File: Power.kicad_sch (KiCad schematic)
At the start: 30 parts, among them J201 Screw_Terminal_01x02_P5mm, J202 USB-C_304A-ACP16X, U201 TPS5430DDA, U202 NUCLEO64-H503RB

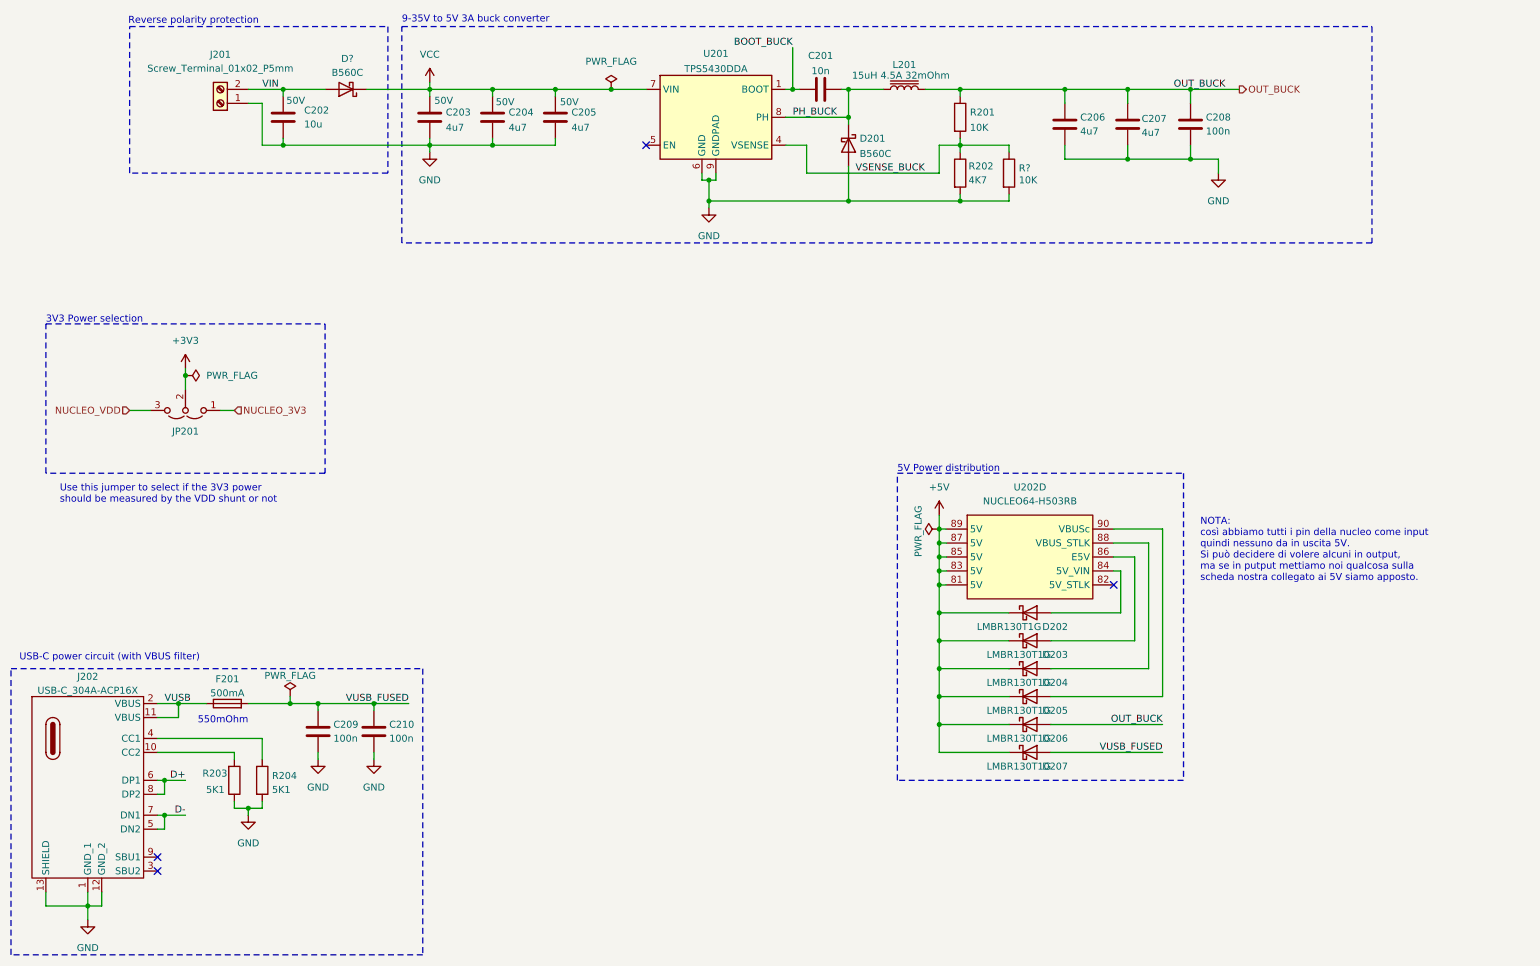
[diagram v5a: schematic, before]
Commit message: Created buzzer footprint, and fixed some libraries simbols and footprint
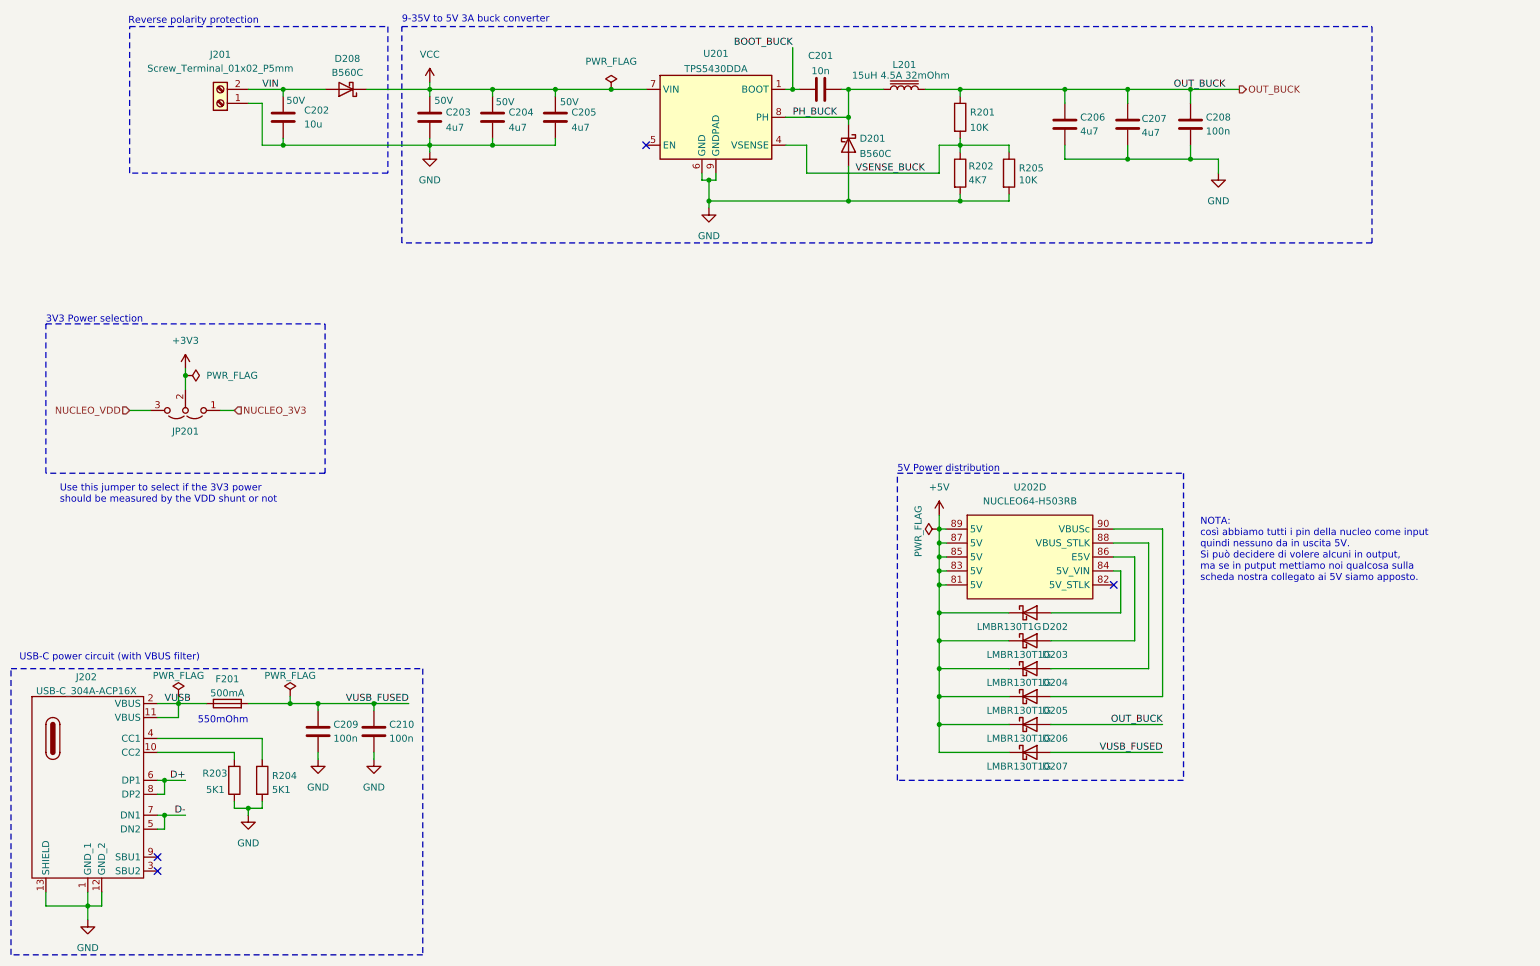
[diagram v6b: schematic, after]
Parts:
- J202: footprint _MIA footprint:USB_C_304A-ACP16X -> ProjectConnectors:USB_C_304A-ACP16X; symbol _MIA:USB-C_304A-ACP16X -> ProjectConnectors:USB-C_304A-ACP16X
- gave numbers to parts that had none: 2
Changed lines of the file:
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@@
 	(wire
 		(pts
+			(xy 49.53 143.51) (xy 49.53 144.78)
+		)
+		(stroke
+			(width 0)
+			(type default)
+		)
+	)
+	(wire
+		(pts
 			(xy 160.02 43.18) (xy 163.83 43.18)
 		)
@@
 	)
 	(symbol
+		(lib_id "power:PWR_FLAG")
+		(at 49.53 143.51 0)
+		(unit 1)
+		(exclude_from_sim no)
+		(in_bom yes)
+		(on_board yes)
+		(dnp no)
+		(property "Reference" "#FLG0205"
+			(at 49.53 141.605 0)
+			(effects
+				(font
+					(size 1.27 1.27)
+				)
+				(hide yes)
+			)
+		)
+		(property "Value" "PWR_FLAG"
+			(at 49.53 139.7 0)
+			(effects
+				(font
+					(size 1.27 1.27)
+				)
+			)
+		)
+		(property "Footprint" ""
+			(at 49.53 143.51 0)
+			(effects
+				(font
+					(size 1.27 1.27)
+				)
+				(hide yes)
+			)
+		)
+		(property "Datasheet" "~"
+			(at 49.53 143.51 0)
+			(effects
+				(font
+					(size 1.27 1.27)
+				)
+				(hide yes)
+			)
+		)
+		(property "Description" "Special symbol for telling ERC where power comes from"
+			(at 49.53 143.51 0)
+			(effects
+				(font
+					(size 1.27 1.27)
+				)
+				(hide yes)
+			)
+		)
+		(pin "1"
+		)
+		(instances
+			(project "Educational-Board_MainBoard"
+				(path "/835b4df9-7d62-45f4-81d2-5a64fbc86f3c/a1b70c1b-93fd-432d-b3bf-990581065c7c"
+					(reference "#FLG0205")
+					(unit 1)
+				)
+			)
+		)
+	)
+	(symbol
 		(lib_name "PWR_FLAG_1")
 		(lib_id "power:PWR_FLAG")
@@
 	)
 	(symbol
-		(lib_id "_MIA:USB-C_304A-ACP16X")
+		(lib_id "ProjectConnectors:USB-C_304A-ACP16X")
 		(at 33.02 158.75 0)
 		(unit 1)
@@
 		(on_board yes)
 		(dnp no)
-		(fields_autoplaced yes)
 		(property "Reference" "J202"
-			(at 33.02 139.861 0)
+			(at 32.766 139.954 0)
 			(effects
 				(font
@@
 		)
 		(property "Value" "USB-C_304A-ACP16X"
-			(at 33.02 142.3979 0)
+			(at 32.766 142.494 0)
 			(effects
 				(font
@@
 			)
 		)
-		(property "Footprint" "_MIA footprint:USB_C_304A-ACP16X"
+		(property "Footprint" "ProjectConnectors:USB_C_304A-ACP16X"
 			(at 33.02 156.21 0)
 			(effects
@@
 					(size 1.27 1.27)
 				)
+				(hide yes)
 			)
 		)
@@
 		(on_board yes)
 		(dnp no)
-		(property "Reference" "R?"
+		(property "Reference" "R205"
 			(at 202.438 47.3515 0)
 			(effects
@@
 			(project "Educational-Board_MainBoard"
 				(path "/835b4df9-7d62-45f4-81d2-5a64fbc86f3c/a1b70c1b-93fd-432d-b3bf-990581065c7c"
-					(reference "R?")
+					(reference "R205")
 					(unit 1)
 				)
@@
 		(on_board yes)
 		(dnp no)
-		(property "Reference" "D?"
+		(property "Reference" "D208"
 			(at 80.264 27.432 0)
 			(effects
@@
 			(project "Educational-Board_MainBoard"
 				(path "/835b4df9-7d62-45f4-81d2-5a64fbc86f3c/a1b70c1b-93fd-432d-b3bf-990581065c7c"
-					(reference "D?")
+					(reference "D208")
 					(unit 1)
 				)

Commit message: Finished the sourcing of the components
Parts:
- L201: now not fitted
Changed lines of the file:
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@@
 		)
 		(instances
-			(project ""
+			(project "Educational-Board_MainBoard"
 				(path "/835b4df9-7d62-45f4-81d2-5a64fbc86f3c/a1b70c1b-93fd-432d-b3bf-990581065c7c"
 					(reference "#PWR0201")
@@
 		)
 		(property "Value" "LMBR130T1G"
-			(at 202.438 135.89 0)
+			(at 199.39 135.89 0)
 			(effects
 				(font
@@
 		)
 		(property "Value" "LMBR130T1G"
-			(at 200.66 130.81 0)
+			(at 199.39 130.81 0)
 			(effects
 				(font
@@
 		)
 		(property "Value" "LMBR130T1G"
-			(at 202.438 146.05 0)
+			(at 199.39 146.05 0)
 			(effects
 				(font
@@
 		)
 		(instances
-			(project ""
+			(project "Educational-Board_MainBoard"
 				(path "/835b4df9-7d62-45f4-81d2-5a64fbc86f3c/a1b70c1b-93fd-432d-b3bf-990581065c7c"
 					(reference "#PWR0205")
@@
 		)
 		(instances
-			(project ""
+			(project "Educational-Board_MainBoard"
 				(path "/835b4df9-7d62-45f4-81d2-5a64fbc86f3c/a1b70c1b-93fd-432d-b3bf-990581065c7c"
 					(reference "#FLG0204")
@@
 		)
 		(instances
-			(project ""
+			(project "Educational-Board_MainBoard"
 				(path "/835b4df9-7d62-45f4-81d2-5a64fbc86f3c/a1b70c1b-93fd-432d-b3bf-990581065c7c"
 					(reference "JP201")
@@
 		)
 		(property "Value" "LMBR130T1G"
-			(at 202.438 140.97 0)
+			(at 199.39 140.97 0)
 			(effects
 				(font
@@
 		)
 		(instances
-			(project ""
+			(project "Educational-Board_MainBoard"
 				(path "/835b4df9-7d62-45f4-81d2-5a64fbc86f3c/a1b70c1b-93fd-432d-b3bf-990581065c7c"
 					(reference "J201")
@@
 		)
 		(instances
-			(project ""
+			(project "Educational-Board_MainBoard"
 				(path "/835b4df9-7d62-45f4-81d2-5a64fbc86f3c/a1b70c1b-93fd-432d-b3bf-990581065c7c"
 					(reference "#FLG0201")
@@
 		)
 		(instances
-			(project ""
+			(project "Educational-Board_MainBoard"
 				(path "/835b4df9-7d62-45f4-81d2-5a64fbc86f3c/a1b70c1b-93fd-432d-b3bf-990581065c7c"
 					(reference "#PWR0206")
@@
 		)
 		(instances
-			(project ""
+			(project "Educational-Board_MainBoard"
 				(path "/835b4df9-7d62-45f4-81d2-5a64fbc86f3c/a1b70c1b-93fd-432d-b3bf-990581065c7c"
 					(reference "U202")
@@
 		(in_bom yes)
 		(on_board yes)
-		(dnp no)
+		(dnp yes)
 		(property "Reference" "L201"
 			(at 181.61 28.5455 90)
@@
 		)
 		(property "Value" "LMBR130T1G"
-			(at 202.438 151.13 0)
+			(at 199.39 151.13 0)
 			(effects
 				(font
@@
 		)
 		(instances
-			(project ""
+			(project "Educational-Board_MainBoard"
 				(path "/835b4df9-7d62-45f4-81d2-5a64fbc86f3c/a1b70c1b-93fd-432d-b3bf-990581065c7c"
 					(reference "#PWR0202")
@@
 		)
 		(property "Value" "LMBR130T1G"
-			(at 202.438 156.21 0)
+			(at 198.12 156.21 0)
 			(effects
 				(font

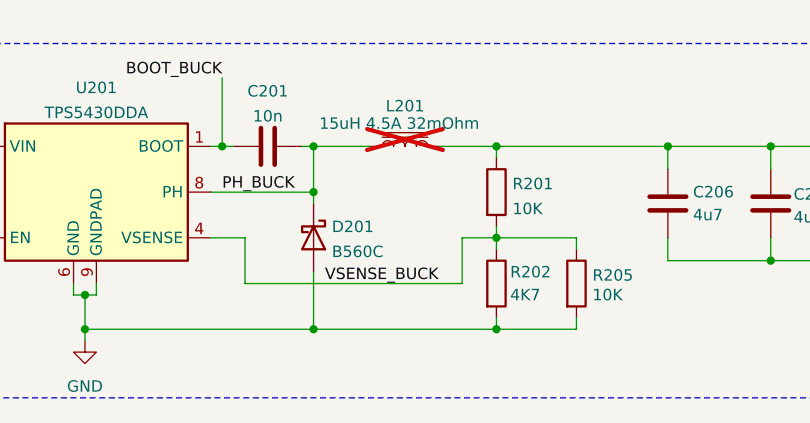
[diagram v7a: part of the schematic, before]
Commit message: Started the checking of the components
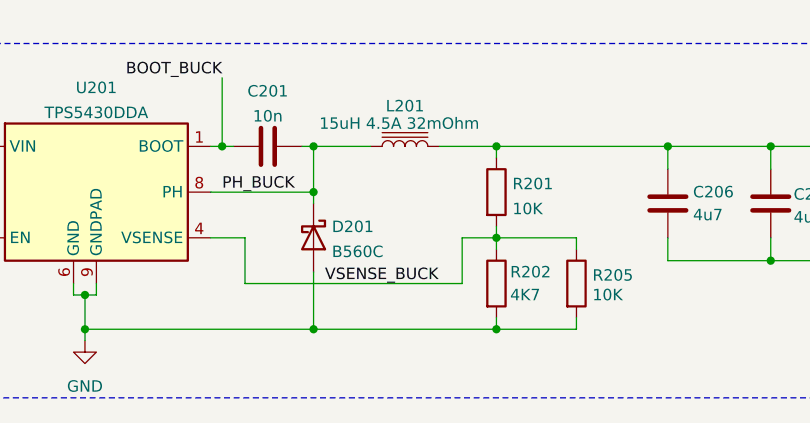
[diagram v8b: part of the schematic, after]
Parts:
- C201, C202, C203, C204, C205, C206, C207, C208, C209, C210, D201, D202, D203, D204, D205, D206, D207, D208, J201, JP201, R201, R203, R204, R205: Checked (none) -> OK
- F201: Checked (none) -> To check value
- L201: Checked (none) -> OK; now fitted
- R202: Checked (none) -> 1K8??
- U201: Checked (none) -> Footprint
